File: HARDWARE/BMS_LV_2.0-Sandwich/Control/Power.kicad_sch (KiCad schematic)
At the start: 25 parts, among them IC1 TAR5S33UTE85LF, IC4 TPS54202HDDCR

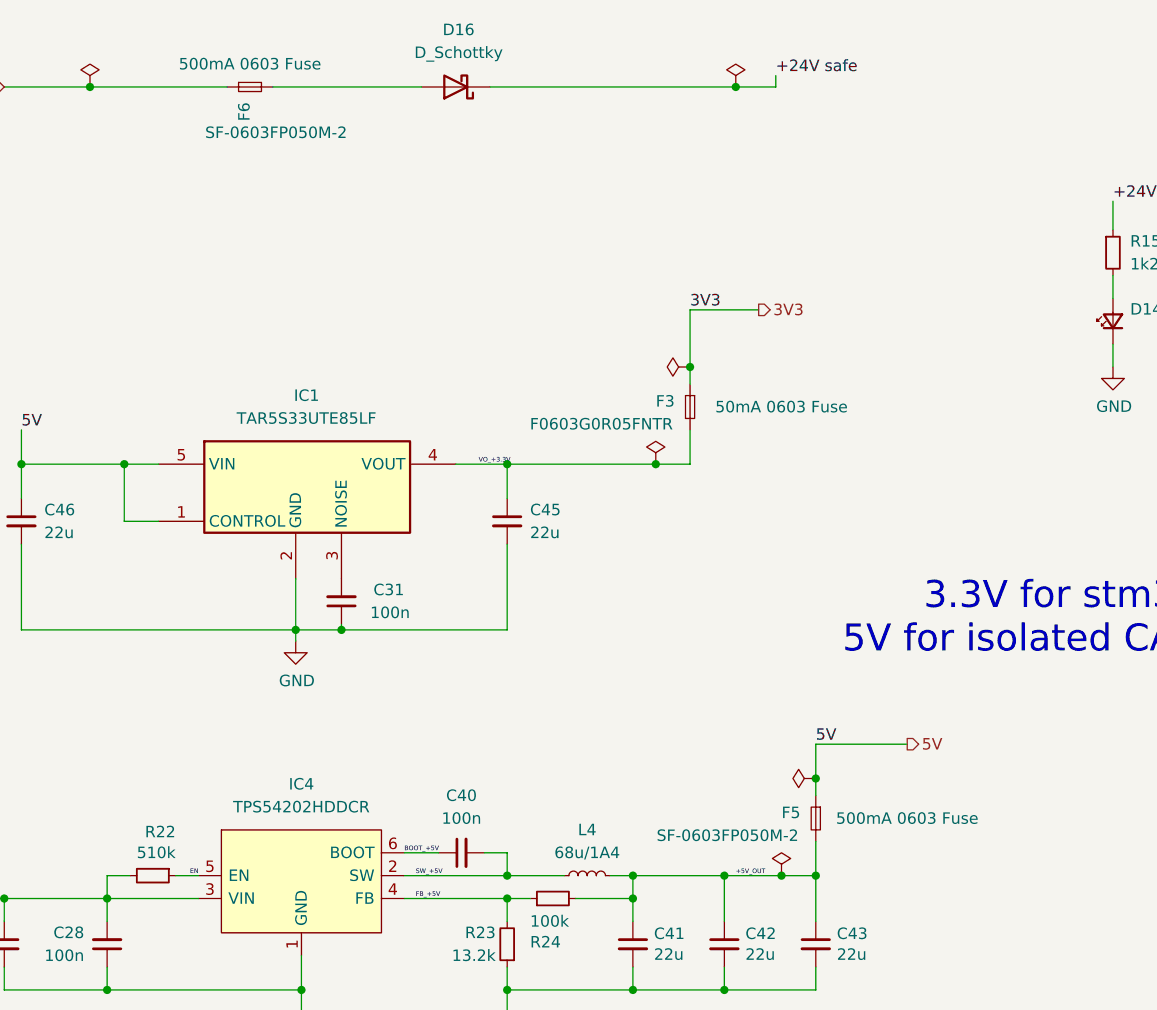
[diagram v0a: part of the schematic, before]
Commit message: Zmiany w power: nowe bezpieczniki, nowy wymienialny layout dla tych bezpiecznikow, dodano diode zenera dla stabilizacji napięcia, zmiany dla control:  wyjebany eeprom, przesunięty can, zmieniony layout przetwornic, dodano programator i tvs, jeszcze do dokonczenia routing w control.
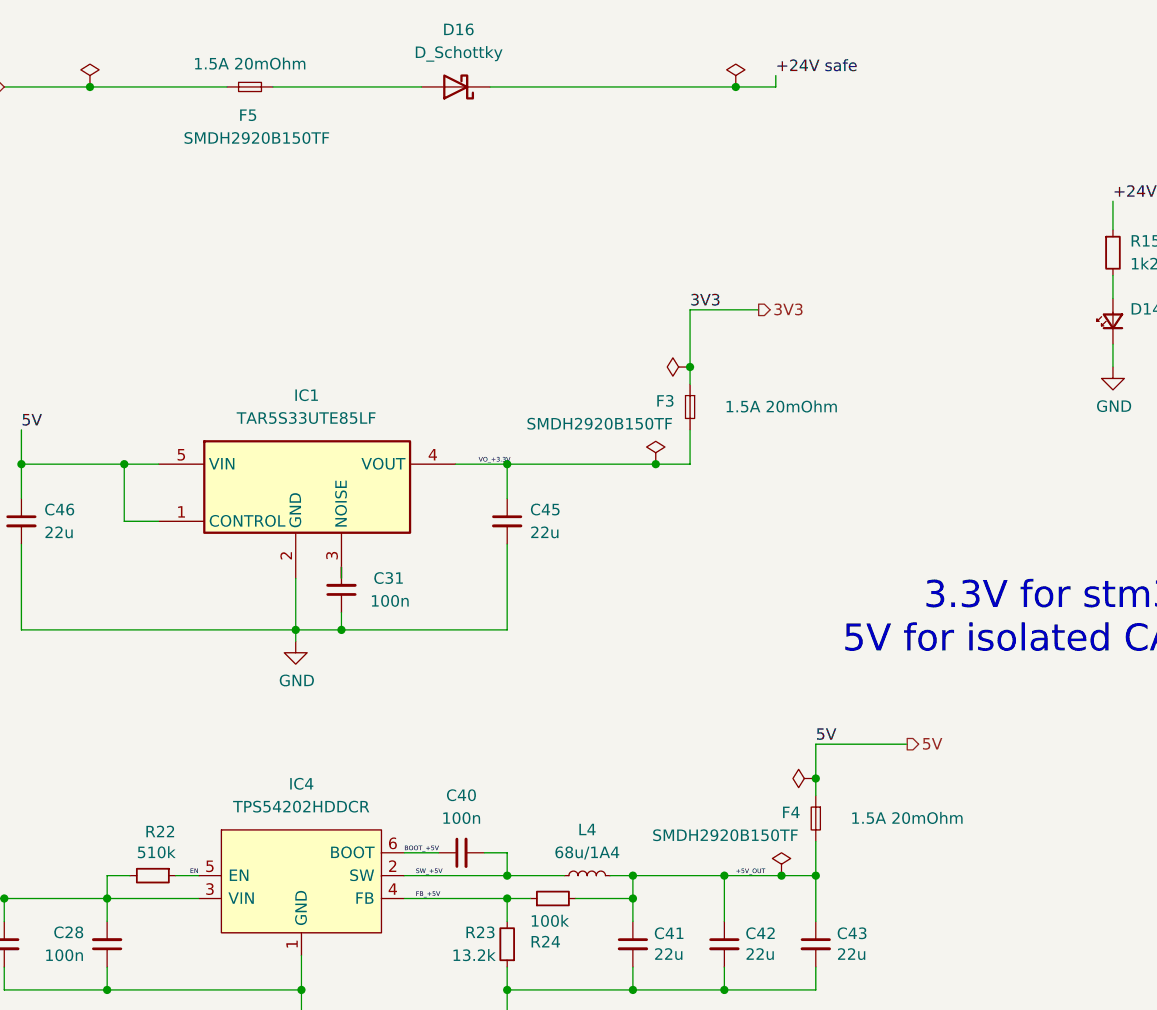
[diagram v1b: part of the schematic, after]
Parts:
- removed F6: SF-0603FP050M-2, Fuse:Fuse_0603_1608Metric_Pad1.05x0.95mm_HandSolder, symbol Device:Fuse_Small
- added F4: SMDH2920B150TF, Fuse:Fuse_2920_7451Metric_Pad2.10x5.45mm_HandSolder, symbol Device:Fuse_Small
- F3: value F0603G0R05FNTR -> SMDH2920B150TF; footprint Fuse:Fuse_0603_1608Metric_Pad1.05x0.95mm_HandSolder -> Fuse:Fuse_2920_7451Metric_Pad2.10x5.45mm_HandSolder
- F5: value SF-0603FP050M-2 -> SMDH2920B150TF; footprint Fuse:Fuse_0603_1608Metric_Pad1.05x0.95mm_HandSolder -> Fuse:Fuse_2920_7451Metric_Pad2.10x5.45mm_HandSolder
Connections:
- net +24V: now also F5.1
- net +5V_OUT: now also F4.2; no longer F5.2
- net 5V: now also F4.1; no longer F5.1
- net at D16.2 (A): now also F5.2
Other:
- moved on the sheet: C31
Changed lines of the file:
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@@
 	(wire
 		(pts
+			(xy 99.06 94.615) (xy 99.06 95.885)
+		)
+		(stroke
+			(width 0)
+			(type default)
+		)
+	)
+	(wire
+		(pts
 			(xy 141.605 141.605) (xy 131.445 141.605)
 		)
@@
 	(wire
 		(pts
-			(xy 99.06 100.965) (xy 99.06 101.6)
+			(xy 99.06 99.695) (xy 99.06 101.6)
 		)
 		(stroke
@@
 	)
 	(symbol
-		(lib_id "Device:Fuse_Small")
-		(at 151.765 122.555 270)
-		(unit 1)
-		(exclude_from_sim no)
-		(in_bom yes)
-		(on_board yes)
-		(dnp no)
-		(property "Reference" "F5"
-			(at 147.955 121.92 90)
-			(effects
-				(font
-					(size 1.27 1.27)
-				)
-				(justify left)
-			)
-		)
-		(property "Value" "SF-0603FP050M-2"
-			(at 149.86 124.46 90)
-			(effects
-				(font
-					(size 1.27 1.27)
-				)
-				(justify right)
-			)
-		)
-		(property "Footprint" "Fuse:Fuse_0603_1608Metric_Pad1.05x0.95mm_HandSolder"
-			(at 151.765 122.555 0)
-			(effects
-				(font
-					(size 1.27 1.27)
-				)
-				(justify left)
-				(hide yes)
-			)
-		)
-		(property "Datasheet" "https://www.mouser.pl/ProductDetail/Bourns/SF-0603FP050M-2?qs=fAHHVMwC%252BbjmUEdZYoiM2w%3D%3D"
-			(at 151.765 122.555 0)
-			(effects
-				(font
-					(size 1.27 1.27)
-				)
-				(hide yes)
-			)
-		)
-		(property "Description" "500mA 0603 Fuse"
-			(at 161.925 122.555 90)
-			(effects
-				(font
-					(size 1.27 1.27)
-				)
-			)
-		)
-		(pin "2"
-		)
-		(pin "1"
-		)
-		(instances
-			(project "BMS_LV_2026_Control"
-				(path "/61cadedd-f367-4fd1-937a-9fd9456f4804/69df93bd-9473-41c8-b75c-1c01f11397f2"
-					(reference "F5")
-					(unit 1)
-				)
-			)
-		)
-	)
-	(symbol
 		(lib_id "Device:D_Schottky")
 		(at 111.76 41.275 180)
@@
 			)
 		)
-		(property "Value" "F0603G0R05FNTR"
+		(property "Value" "SMDH2920B150TF"
 			(at 135.89 78.74 90)
 			(effects
@@
 			)
 		)
-		(property "Footprint" "Fuse:Fuse_0603_1608Metric_Pad1.05x0.95mm_HandSolder"
+		(property "Footprint" "Fuse:Fuse_2920_7451Metric_Pad2.10x5.45mm_HandSolder"
 			(at 137.795 76.835 0)
 			(effects
@@
 			)
 		)
-		(property "Datasheet" "https://www.mouser.pl/ProductDetail/Kamaya/FCCR16151ABTP?qs=iLbezkQI%252BsgGZHcPKnwGpQ%3D%3D"
+		(property "Datasheet" "https://www.mouser.pl/ProductDetail/YAGEO/SMDH2920B150TF?qs=jcD%2FCkGBYeMJsuSx6iuINA%3D%3D"
 			(at 137.795 76.835 0)
 			(effects
@@
 			)
 		)
-		(property "Description" "50mA 0603 Fuse"
+		(property "Description" "1.5A 20mOhm"
 			(at 147.955 76.835 90)
 			(effects
@@
 	)
 	(symbol
+		(lib_id "Device:Fuse_Small")
+		(at 151.765 122.555 270)
+		(unit 1)
+		(exclude_from_sim no)
+		(in_bom yes)
+		(on_board yes)
+		(dnp no)
+		(property "Reference" "F4"
+			(at 147.955 121.92 90)
+			(effects
+				(font
+					(size 1.27 1.27)
+				)
+				(justify left)
+			)
+		)
+		(property "Value" "SMDH2920B150TF"
+			(at 149.86 124.46 90)
+			(effects
+				(font
+					(size 1.27 1.27)
+				)
+				(justify right)
+			)
+		)
+		(property "Footprint" "Fuse:Fuse_2920_7451Metric_Pad2.10x5.45mm_HandSolder"
+			(at 151.765 122.555 0)
+			(effects
+				(font
+					(size 1.27 1.27)
+				)
+				(justify left)
+				(hide yes)
+			)
+		)
+		(property "Datasheet" "https://www.mouser.pl/ProductDetail/YAGEO/SMDH2920B150TF?qs=jcD%2FCkGBYeMJsuSx6iuINA%3D%3D"
+			(at 151.765 122.555 0)
+			(effects
+				(font
+					(size 1.27 1.27)
+				)
+				(hide yes)
+			)
+		)
+		(property "Description" "1.5A 20mOhm"
+			(at 161.925 122.555 90)
+			(effects
+				(font
+					(size 1.27 1.27)
+				)
+			)
+		)
+		(pin "2"
+		)
+		(pin "1"
+		)
+		(instances
+			(project "BMS_LV_2026_Control"
+				(path "/61cadedd-f367-4fd1-937a-9fd9456f4804/69df93bd-9473-41c8-b75c-1c01f11397f2"
+					(reference "F4")
+					(unit 1)
+				)
+			)
+		)
+	)
+	(symbol
 		(lib_id "Device:R_Small")
 		(at 184.785 59.69 0)
@@
 	)
 	(symbol
-		(lib_id "Device:Fuse_Small")
-		(at 88.9 41.275 0)
-		(unit 1)
-		(exclude_from_sim no)
-		(in_bom yes)
-		(on_board yes)
-		(dnp no)
-		(property "Reference" "F6"
-			(at 88.265 45.085 90)
-			(effects
-				(font
-					(size 1.27 1.27)
-				)
-				(justify left)
-			)
-		)
-		(property "Value" "SF-0603FP050M-2"
-			(at 99.695 46.355 0)
-			(effects
-				(font
-					(size 1.27 1.27)
-				)
-				(justify right)
-			)
-		)
-		(property "Footprint" "Fuse:Fuse_0603_1608Metric_Pad1.05x0.95mm_HandSolder"
-			(at 88.9 41.275 0)
-			(effects
-				(font
-					(size 1.27 1.27)
-				)
-				(justify left)
-				(hide yes)
-			)
-		)
-		(property "Datasheet" "https://www.mouser.pl/ProductDetail/Bourns/SF-0603FP050M-2?qs=fAHHVMwC%252BbjmUEdZYoiM2w%3D%3D"
-			(at 88.9 41.275 0)
-			(effects
-				(font
-					(size 1.27 1.27)
-				)
-				(hide yes)
-			)
-		)
-		(property "Description" "500mA 0603 Fuse"
-			(at 88.9 38.735 0)
-			(effects
-				(font
-					(size 1.27 1.27)
-				)
-			)
-		)
-		(pin "2"
-		)
-		(pin "1"
-		)
-		(instances
-			(project "BMS_LV_2026_Control"
-				(path "/61cadedd-f367-4fd1-937a-9fd9456f4804/69df93bd-9473-41c8-b75c-1c01f11397f2"
-					(reference "F6")
-					(unit 1)
-				)
-			)
-		)
-	)
-	(symbol
 		(lib_id "SamacsysNew:TPS54202HDDCR")
 		(at 97.155 128.905 0)
@@
 	(symbol
 		(lib_id "Device:C_Small")
-		(at 99.06 98.425 180)
+		(at 99.06 97.155 180)
 		(unit 1)
 		(exclude_from_sim no)
@@
 		(dnp no)
 		(property "Reference" "C31"
-			(at 106.045 97.155 0)
+			(at 106.045 95.885 0)
 			(effects
 				(font
@@
 		)
 		(property "Value" "100n"
-			(at 106.68 99.695 0)
+			(at 106.68 98.425 0)
 			(effects
 				(font
@@
 		)
 		(property "Footprint" "Capacitor_SMD:C_0603_1608Metric"
-			(at 99.06 98.425 0)
+			(at 99.06 97.155 0)
 			(effects
 				(font
@@
 		)
 		(property "Datasheet" "https://www.mouser.pl/datasheet/2/281/1/GRM033R6YA104ME14_01A-1982036.pdf"
-			(at 99.06 98.425 0)
+			(at 99.06 97.155 0)
 			(effects
 				(font
@@
 		)
 		(property "Description" ""
-			(at 99.06 98.425 0)
+			(at 99.06 97.155 0)
 			(effects
 				(font
@@
 		)
 		(property "Manufacturer_Name" "--"
-			(at 99.06 98.425 0)
+			(at 99.06 97.155 0)
 			(effects
 				(font
@@
 		)
 		(property "Manufacturer_Part_Number" "C0603C104J3RACTU"
-			(at 99.06 98.425 0)
+			(at 99.06 97.155 0)
 			(effects
 				(font
@@
 		)
 		(property "In Order" ""
-			(at 99.06 98.425 0)
+			(at 99.06 97.155 0)
 			(effects
 				(font
@@
 		)
 		(property "Mouser Part Number" "80-C0603C104J3R"
-			(at 99.06 98.425 0)
+			(at 99.06 97.155 0)
 			(effects
 				(font
@@
 		)
 		(property "Mouser Price/Stock" "https://www.mouser.pl/ProductDetail/Murata-Electronics/GRM033R6YA104ME14D?qs=P%2FC4Eoq9CDwjSVlAMBrT%252Bw%3D%3D"
-			(at 99.06 98.425 0)
+			(at 99.06 97.155 0)
 			(effects
 				(font
@@
 		)
 		(property "Author" ""
-			(at 99.06 98.425 0)
+			(at 99.06 97.155 0)
 			(effects
 				(font
@@
 		)
 		(property "License" ""
-			(at 99.06 98.425 0)
+			(at 99.06 97.155 0)
 			(effects
 				(font
@@
 		)
 		(property "MPN" ""
-			(at 99.06 98.425 0)
+			(at 99.06 97.155 0)
 			(effects
 				(font
@@
 		)
 		(property "Manufacturer" ""
-			(at 99.06 98.425 0)
+			(at 99.06 97.155 0)
 			(effects
 				(font
@@
 		)
 		(property "Sim.Pins" ""
-			(at 99.06 98.425 0)
+			(at 99.06 97.155 0)
 			(effects
 				(font
@@
 					(unit 1)
 				)
+			)
+		)
+	)
+	(symbol
+		(lib_id "Device:Fuse_Small")
+		(at 88.9 41.275 0)
+		(unit 1)
+		(exclude_from_sim no)
+		(in_bom yes)
+		(on_board yes)
+		(dnp no)
+		(property "Reference" "F5"
+			(at 87.63 44.45 0)
+			(effects
+				(font
+					(size 1.27 1.27)
+				)
+				(justify left)
+			)
+		)
+		(property "Value" "SMDH2920B150TF"
+			(at 97.79 46.99 0)
+			(effects
+				(font
+					(size 1.27 1.27)
+				)
+				(justify right)
+			)
+		)
+		(property "Footprint" "Fuse:Fuse_2920_7451Metric_Pad2.10x5.45mm_HandSolder"
+			(at 88.9 41.275 0)
+			(effects
+				(font
+					(size 1.27 1.27)
+				)
+				(justify left)
+				(hide yes)
+			)
+		)
+		(property "Datasheet" "https://www.mouser.pl/ProductDetail/YAGEO/SMDH2920B150TF?qs=jcD%2FCkGBYeMJsuSx6iuINA%3D%3D"
+			(at 88.9 41.275 0)
+			(effects
+				(font
+					(size 1.27 1.27)
+				)
+				(hide yes)
+			)
+		)
+		(property "Description" "1.5A 20mOhm"
+			(at 88.9 38.735 0)
+			(effects
+				(font
+					(size 1.27 1.27)
+				)
+			)
+		)
+		(pin "2"
+		)
+		(pin "1"
+		)
+		(instances
+			(project "BMS_LV_2026_Control"
+				(path "/61cadedd-f367-4fd1-937a-9fd9456f4804/69df93bd-9473-41c8-b75c-1c01f11397f2"
+					(reference "F5")
+					(unit 1)
+				)

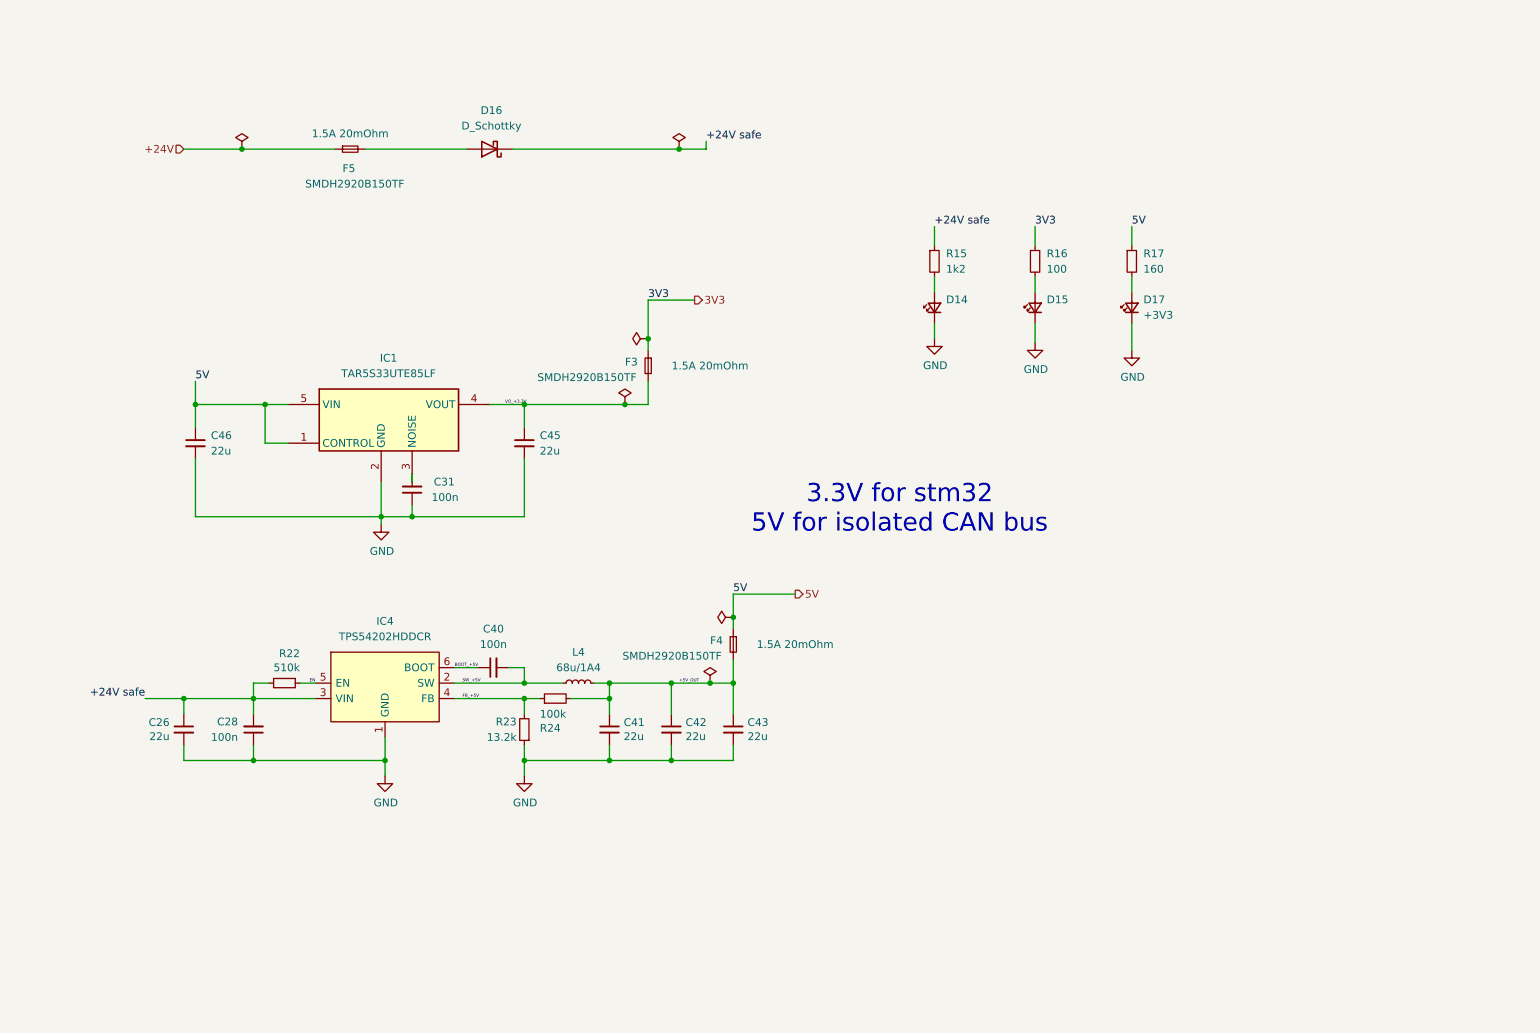
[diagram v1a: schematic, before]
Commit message: Pierwsza wersja bez błędów DRC/ERC, skończony routing plytki control
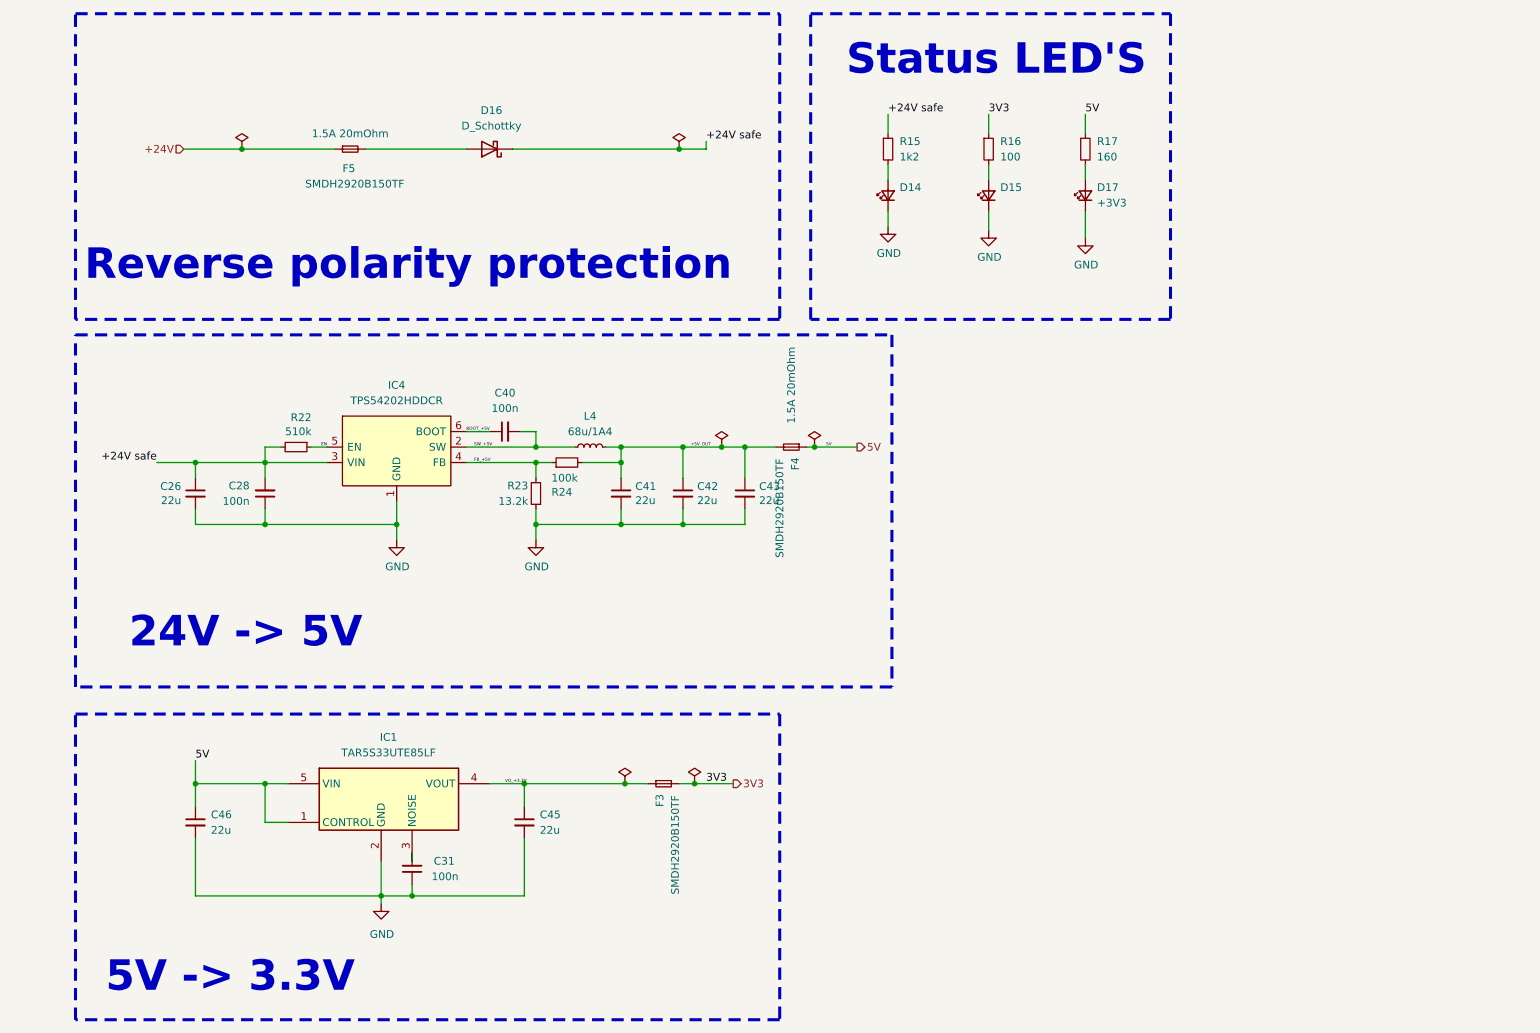
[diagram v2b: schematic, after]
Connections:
- net 3V3: now also F3.2; no longer F3.1
- net VO_+3.3V: now also F3.1; no longer F3.2
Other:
- note added: "24V -> 5V"
- note added: "5V -> 3.3V"
- note added: "Reverse polarity protection"
- note added: "Status LED'S"
- note removed: "3.3V for stm32 5V for isolated CAN bus"
- moved on the sheet: C26, C28, C31, C40, C41, C42, C43, C45, C46, D14, D15, D17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

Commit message: Ulozono silkscreena
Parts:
- added C57, C59: 22u, Capacitor_SMD:C_0805_2012Metric_Pad1.18x1.45mm_HandSolder, symbol Device:C_Small
- added C58: 100n, Capacitor_SMD:C_0603_1608Metric, symbol Device:C_Small
- added D18: ~, LED_SMD:LED_0603_1608Metric_Pad1.05x0.95mm_HandSolder, symbol Device:LED_Small
- added F6: SMDH2920B150TF, Fuse:Fuse_2920_7451Metric_Pad2.10x5.45mm_HandSolder, symbol Device:Fuse_Small
- added IC2: TAR5S33UTE85LF, Footprint:SOTFL65P210X75-5N, symbol TAR5S33UTE85LF:TAR5S33UTE85LF
- added R18: 100, Resistor_SMD:R_0603_1608Metric_Pad0.98x0.95mm_HandSolder, symbol Device:R_Small
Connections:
- net 5V: now also C57.1, IC2.1 (CONTROL), IC2.5 (VIN)
- net GND: now also C57.2, C58.1, C59.2, D18.1 (K), IC2.2 (GND)
- new net: C58.2, IC2.3 (NOISE)
- new net: D18.2 (A), R18.2
- new net 3V3A: F6.2, R18.1
- new net VO_+3.3VA: C59.1, F6.1, IC2.4 (VOUT)
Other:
- note added: "5V -> 3.3V (analog)"

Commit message: Naprawiono: załączanie lv, brak zlącza programatora (XD) oraz brak podłączenia czujnika prądu :9
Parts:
- D14, D15, D18: value ~ -> (none)

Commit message: Dodane zenery, programator w innym miejscu
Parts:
- added D1: SMF26VTFTR, Diode_SMD:D_SOD-123F, symbol Device:D_Zener_Small
- added D2, D3: SMF3.0, Diode_SMD:D_SOD-123F, symbol Device:D_Zener_Small
- added D4: SMF5.0A_R1_00001, Diode_SMD:D_SOD-123F, symbol Device:D_Zener_Small
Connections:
- net +24V safe: now also D1.1 (K)
- net 3V3: now also D3.1 (K)
- net 3V3A: now also D2.1 (K)
- net 5V: now also D4.1 (K)
- net GND: now also D1.2 (A), D2.2 (A), D3.2 (A), D4.2 (A)
